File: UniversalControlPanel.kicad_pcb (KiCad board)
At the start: 2 copper layers, 61 x 40.6 mm, 50 parts, among them J1 USB_B_Micro, J2 Conn_ARM_JTAG_SWD_10, J3 Conn_01x40, J4 Conn_02x03_Odd_Even, Q1 2N7002, Q2 2N7002, Q3 2N7002, Q4 2N7002, U1 LM78M05_TO252, U2 MAX14783ExS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

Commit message: some changes
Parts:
- removed C10, C6, C7: 15nF, Capacitor_SMD:C_0402_1005Metric
- removed C8, C9: 100n, Capacitor_SMD:C_0402_1005Metric
- removed D3, D5, D7: SM4007, Diode_SMD:D_MELF
- removed D4, D6: BAT54C, Package_TO_SOT_SMD:SOT-23
- removed Q1, Q2, Q3, Q4: 2N7002, Package_TO_SOT_SMD:SOT-23
- removed R10, R11: 500, Resistor_SMD:R_0402_1005Metric
- removed R12, R13: 100k, Resistor_SMD:R_0402_1005Metric
- removed R14, R15, R16, R17: R, Resistor_SMD:R_0402_1005Metric
- removed R18: 50, Resistor_SMD:R_0402_1005Metric
- removed U5, U7: LMV321, Package_TO_SOT_SMD:SOT-23-5
- added J5: Conn_01x02, Connector_JST:JST_XH_B2B-XH-A_1x02_P2.50mm_Vertical, F.Cu at (88.9, 64.8)
- D2: value SM4007 -> LED; footprint Diode_SMD:D_MELF -> LED_SMD:LED_0603_1608Metric
- R8: value 100k -> 120; footprint Resistor_SMD:R_0402_1005Metric -> Resistor_SMD:R_0805_2012Metric_Pad1.20x1.40mm_HandSolder
- R9: value 100k -> R
- U6: value ESP32-S2-WROVER-I -> ESP32-S2-WROOM-I
- moved D2 77.9 mm to (102.0, 96.8)
- moved U2 73.6 mm to (100.3, 63.5), turned to 180 degrees
- moved R9 70.4 mm to (105.4, 96.5)
- moved R8 56.6 mm to (95.2, 63.5), turned to 90 degrees
- moved C2 29.3 mm to (62.7, 63.5)
- moved R2 29.3 mm to (83.4, 47.8)
- moved C1 29.3 mm to (74.0, 46.5)
- moved C3 29.3 mm to (83.8, 43.2)
- moved C5 29.3 mm to (89.4, 43.2)
- moved D1 29.3 mm to (78.1, 43.2)
- moved R1 29.3 mm to (76.6, 54.3)
- moved R6 29.3 mm to (83.4, 45.9)
- moved C4 29.3 mm to (71.1, 59.2)
- moved R3 29.3 mm to (76.6, 52.3)
- moved R4 29.3 mm to (79.5, 50.3)
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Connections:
- D2 pad 2: Net-(D2-Pad2) -> unconnected-(D2-Pad2)
- R8 pad 1: PD_OUT_1 -> Net-(U2-Pad7)
- R8 pad 2: GND -> Net-(U2-Pad6)
- R9 pad 1: Net-(Q2-Pad1) -> unconnected-(R9-Pad1)
- R9 pad 2: GND -> unconnected-(R9-Pad2)
- U2 pad 6: unconnected-(U2-Pad6) -> Net-(U2-Pad6)
- U2 pad 7: unconnected-(U2-Pad7) -> Net-(U2-Pad7)
- U6 pad 10: AIN_3.3V -> unconnected-(U6-Pad10)
- U6 pad 11: PD_OUT_1 -> unconnected-(U6-Pad11)
- U6 pad 12: PD_OUT_2 -> unconnected-(U6-Pad12)
- U6 pad 13: PD_OUT_3 -> unconnected-(U6-Pad13)
- U6 pad 14: PD_OUT_4 -> unconnected-(U6-Pad14)
- U6 pad 9: AIN_10V -> unconnected-(U6-Pad9)

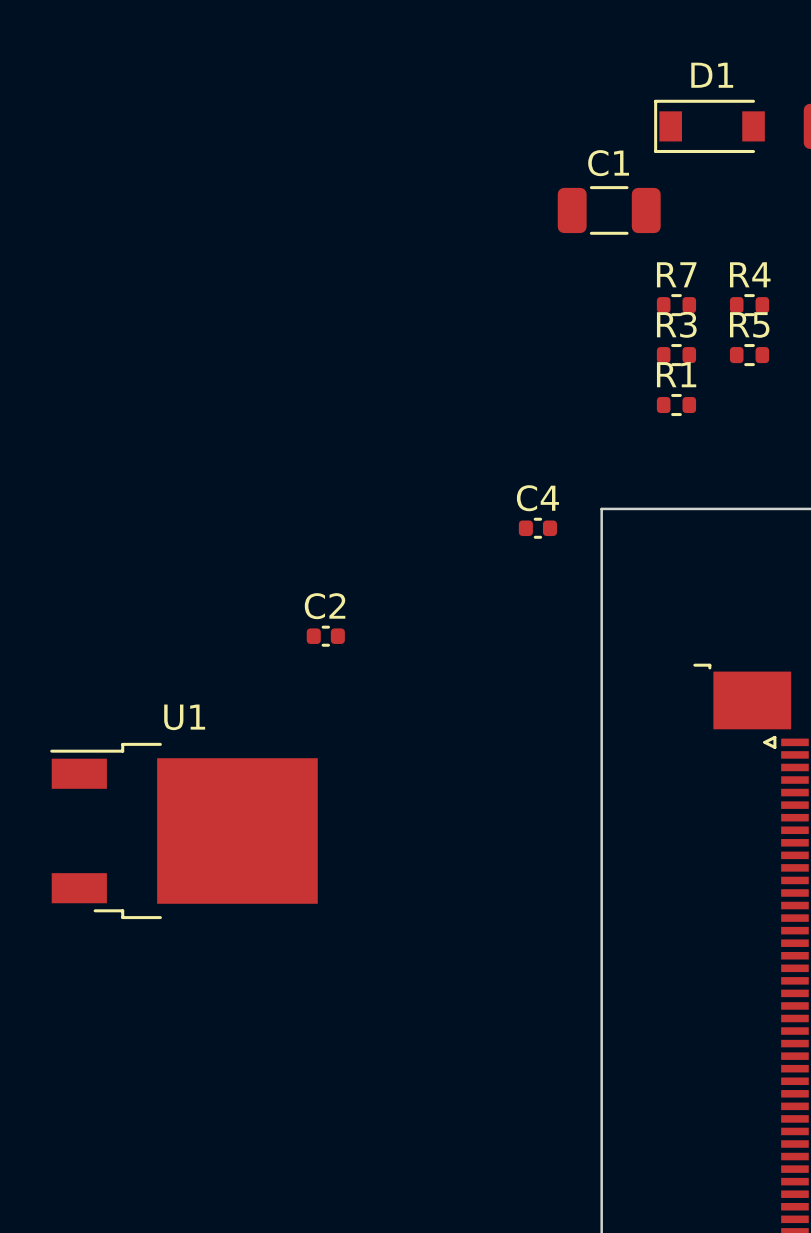
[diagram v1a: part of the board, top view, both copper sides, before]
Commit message: replaced with TSR
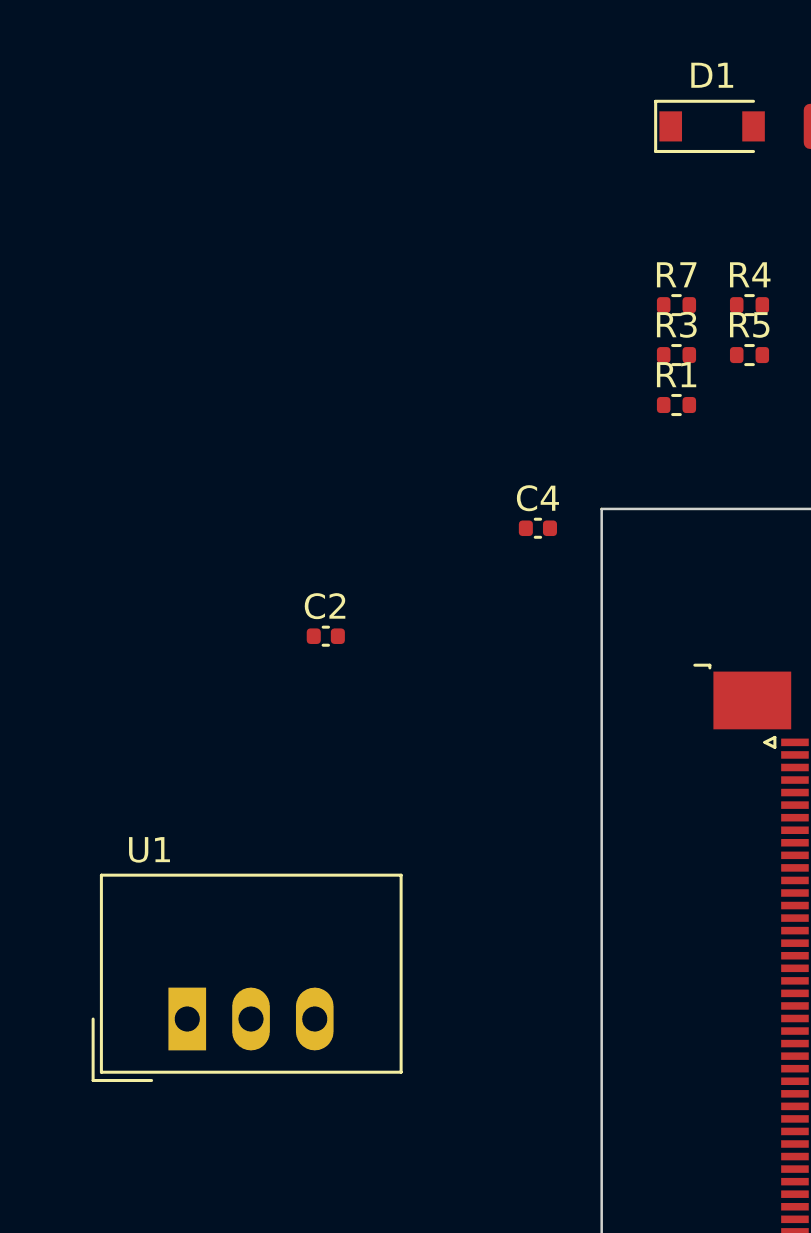
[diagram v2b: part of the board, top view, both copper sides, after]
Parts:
- removed C1: 10u, Capacitor_SMD:C_1206_3216Metric
- U1: value LM78M05_TO252 -> TSR_1-2450; footprint Package_TO_SOT_SMD:TO-252-2 -> Converter_DCDC:Converter_DCDC_TRACO_TSR-1_THT
- moved U1 7.49 mm to (57.1, 78.7)

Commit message: wip
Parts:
- added C1: 100n, Capacitor_SMD:C_0402_1005Metric, F.Cu at (125.0, 85.0)
- added D3: CDSOT23-SM712, Octopart:Bourns_Inc.-SOT23-0-0-IPC_B, F.Cu at (125.7, 122.7)
- added H1: MountingHole, MountingHole:MountingHole_3.5mm, F.Cu at (116.4, 81.2)
- added H2: MountingHole, MountingHole:MountingHole_3.5mm, F.Cu at (116.4, 129.8)
- added J6: 1Wire, Connector_PinHeader_2.54mm:PinHeader_1x03_P2.54mm_Vertical, F.Cu at (129.5, 81.0)
- added R10: 4K7, Resistor_SMD:R_0402_1005Metric, F.Cu at (128.0, 85.0)
- J3: footprint Connector_FFC-FPC:TE_4-1734839-0_1x40-1MP_P0.5mm_Horizontal -> Connector_FFC-FPC:Hirose_FH12-40S-0.5SH_1x40-1MP_P0.50mm_Horizontal
- R9: value R -> 330
- moved U1 105.9 mm to (151.7, 126.4), turned to 90 degrees
- moved C4 75.1 mm to (136.0, 97.0)
- moved R1 75.1 mm to (141.5, 92.1)
- moved R2 75.1 mm to (148.3, 85.7)
- moved R3 75.1 mm to (141.5, 90.1)
- moved R4 75.1 mm to (144.4, 88.1)
- moved R5 75.1 mm to (144.4, 90.1)
- moved R6 75.1 mm to (148.3, 83.7)
- moved R7 75.1 mm to (141.5, 88.1)
- moved C2 75.1 mm to (127.5, 101.3)
- moved C3 75.1 mm to (148.6, 81.0)
- moved C5 75.1 mm to (154.3, 81.0)
- moved D1 75.1 mm to (142.9, 81.0)
- moved J5 74.7 mm to (127.0, 129.0), turned to 180 degrees
- moved D2 69.9 mm to (170.0, 81.0), turned to -90 degrees
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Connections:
- D2 pad 1: unconnected-(D2-Pad1) -> Net-(D2-Pad1)
- D2 pad 2: unconnected-(D2-Pad2) -> Net-(D2-Pad2)
- R9 pad 1: unconnected-(R9-Pad1) -> Net-(D2-Pad1)
- R9 pad 2: unconnected-(R9-Pad2) -> GND
- U6 pad 18: unconnected-(U6-Pad18) -> Net-(D2-Pad2)
- U6 pad 25: unconnected-(U6-Pad25) -> /1WIRE
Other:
- board size 61 x 40.6 mm -> 65 x 55 mm
